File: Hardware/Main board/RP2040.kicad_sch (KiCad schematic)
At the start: 16 parts, among them U4 RP2040

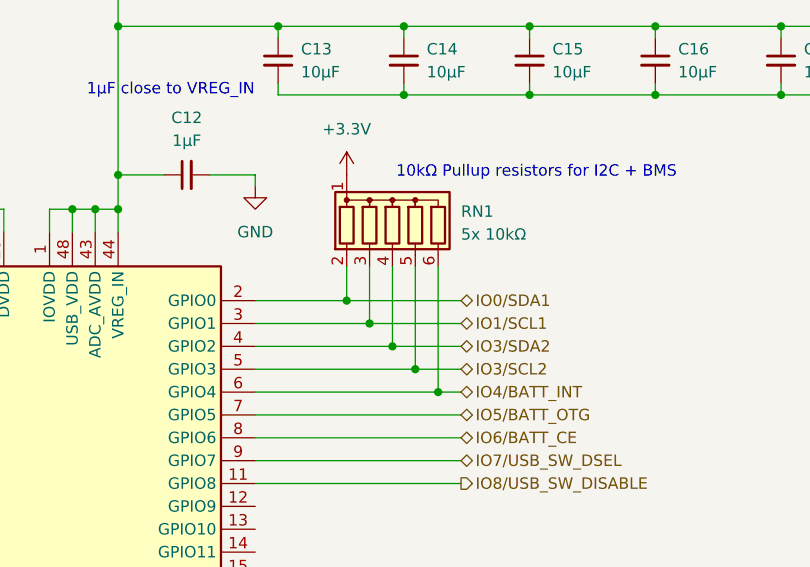
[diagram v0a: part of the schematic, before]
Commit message: Big changes
- Folder changes
- change dimensions of board to match thicker material
- begin part selection/footprint selection
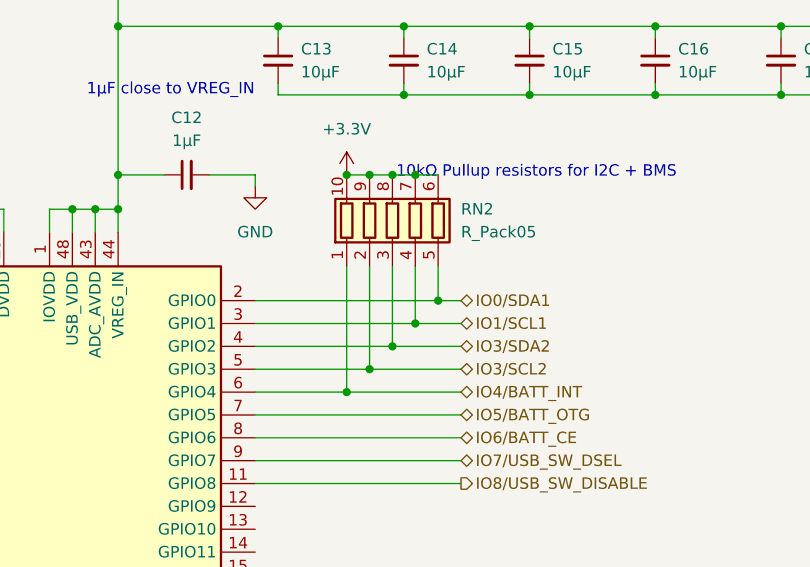
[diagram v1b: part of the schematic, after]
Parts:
- removed RN1: 5x 10kΩ, Resistor_THT:R_Array_SIP6, symbol Device:R_Network05
- added RN2: R_Pack05, Resistor_SMD:R_Array_Convex_5x0603, symbol Device:R_Pack05
- C10, C13, C14, C15, C16, C17, C18, C19, C20, C9: footprint (none) -> Capacitor_SMD:C_0603_1608Metric
- C11, C12: footprint (none) -> Capacitor_SMD:C_0402_1005Metric
- R5, R6: footprint (none) -> Resistor_SMD:R_0603_1608Metric
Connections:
- net +3.3V: now also RN2.10 (R1.2), RN2.6 (R5.2), RN2.7 (R4.2), RN2.8 (R3.2), RN2.9 (R2.2)
- net IO0/SDA1: now also RN2.5 (R5.1)
- net IO1/SCL1: now also RN2.4 (R4.1)
- net IO3/SCL2: now also RN2.2 (R2.1)
- net IO3/SDA2: now also RN2.3 (R3.1)
- net IO4/BATT_INT: now also RN2.1 (R1.1)

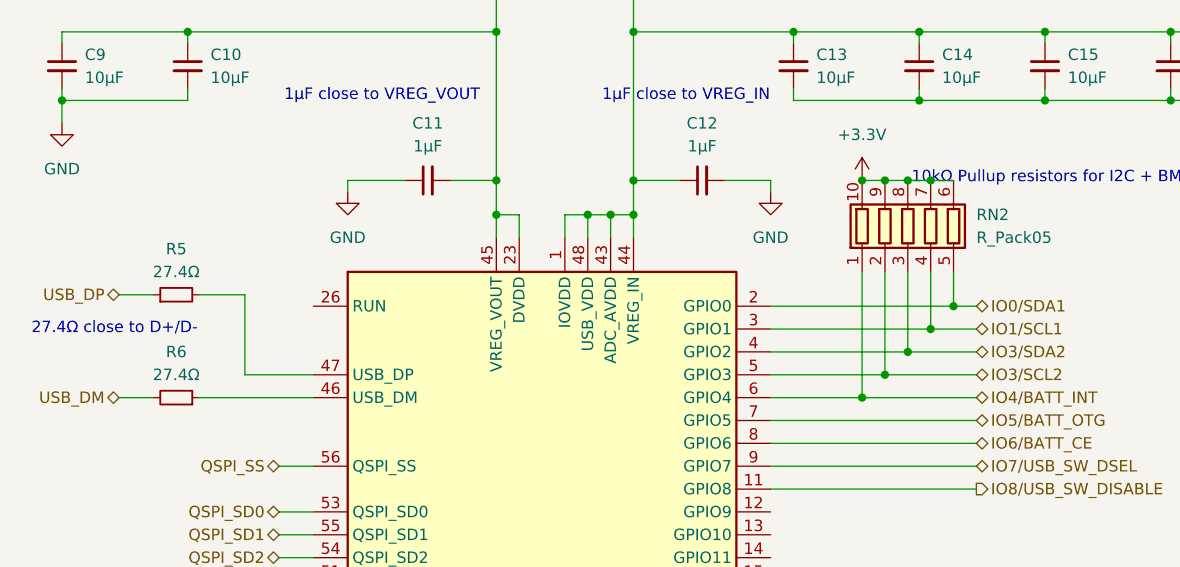
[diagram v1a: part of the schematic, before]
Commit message: Schematic changes
- changed positions/schematic values and nets
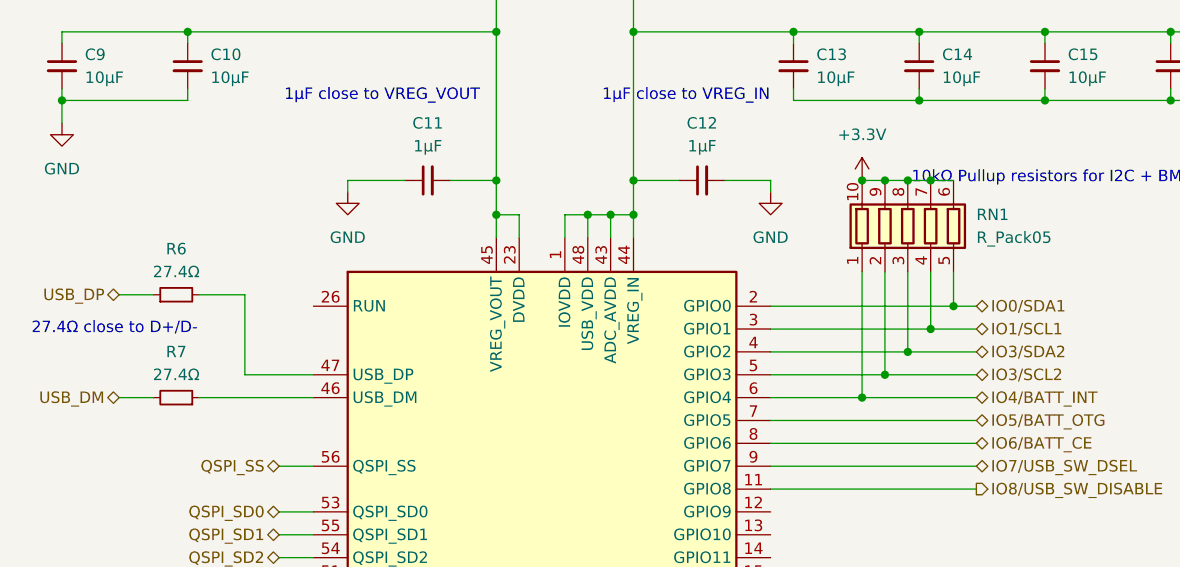
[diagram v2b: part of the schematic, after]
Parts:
- renumbered R5 to R6, R6 to R7, RN2 to RN1
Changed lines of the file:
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@@
 		(dnp no)
 		(fields_autoplaced yes)
-		(property "Reference" "#PWR030"
+		(property "Reference" "#PWR028"
 			(at 106.68 162.56 0)
 			(effects
@@
 			(project "Minibadge Display 5x3"
 				(path "/e5119d15-74fb-4259-abbc-5cab1f368532/9c03ac80-c552-4a59-83c4-4e8b67a63031"
-					(reference "#PWR030")
+					(reference "#PWR028")
 					(unit 1)
 				)
@@
 		(dnp no)
 		(fields_autoplaced yes)
-		(property "Reference" "RN2"
+		(property "Reference" "RN1"
 			(at 154.94 62.2299 0)
 			(effects
@@
 			(project ""
 				(path "/e5119d15-74fb-4259-abbc-5cab1f368532/9c03ac80-c552-4a59-83c4-4e8b67a63031"
-					(reference "RN2")
+					(reference "RN1")
 					(unit 1)
 				)
@@
 		(dnp no)
 		(fields_autoplaced yes)
-		(property "Reference" "#PWR029"
+		(property "Reference" "#PWR027"
 			(at 101.6 38.1 0)
 			(effects
@@
 			(project ""
 				(path "/e5119d15-74fb-4259-abbc-5cab1f368532/9c03ac80-c552-4a59-83c4-4e8b67a63031"
-					(reference "#PWR029")
+					(reference "#PWR027")
 					(unit 1)
 				)
@@
 		(dnp no)
 		(fields_autoplaced yes)
-		(property "Reference" "#PWR033"
+		(property "Reference" "#PWR031"
 			(at 142.24 62.23 0)
 			(effects
@@
 			(project ""
 				(path "/e5119d15-74fb-4259-abbc-5cab1f368532/9c03ac80-c552-4a59-83c4-4e8b67a63031"
-					(reference "#PWR033")
+					(reference "#PWR031")
 					(unit 1)
 				)
@@
 		(dnp no)
 		(fields_autoplaced yes)
-		(property "Reference" "#PWR034"
+		(property "Reference" "#PWR032"
 			(at 232.41 58.42 0)
 			(effects
@@
 			(project ""
 				(path "/e5119d15-74fb-4259-abbc-5cab1f368532/9c03ac80-c552-4a59-83c4-4e8b67a63031"
-					(reference "#PWR034")
+					(reference "#PWR032")
 					(unit 1)
 				)
@@
 		(dnp no)
 		(fields_autoplaced yes)
-		(property "Reference" "#PWR032"
+		(property "Reference" "#PWR030"
 			(at 132.08 66.04 0)
 			(effects
@@
 			(project "Minibadge Display 5x3"
 				(path "/e5119d15-74fb-4259-abbc-5cab1f368532/9c03ac80-c552-4a59-83c4-4e8b67a63031"
-					(reference "#PWR032")
+					(reference "#PWR030")
 					(unit 1)
 				)
@@
 		(on_board yes)
 		(dnp no)
-		(property "Reference" "R6"
+		(property "Reference" "R7"
 			(at 66.04 77.47 90)
 			(effects
@@
 			(project ""
 				(path "/e5119d15-74fb-4259-abbc-5cab1f368532/9c03ac80-c552-4a59-83c4-4e8b67a63031"
-					(reference "R6")
+					(reference "R7")
 					(unit 1)
 				)
@@
 		(dnp no)
 		(fields_autoplaced yes)
-		(property "Reference" "#PWR028"
+		(property "Reference" "#PWR026"
 			(at 85.09 66.04 0)
 			(effects
@@
 			(project "Minibadge Display 5x3"
 				(path "/e5119d15-74fb-4259-abbc-5cab1f368532/9c03ac80-c552-4a59-83c4-4e8b67a63031"
-					(reference "#PWR028")
+					(reference "#PWR026")
 					(unit 1)
 				)
@@
 		(dnp no)
 		(fields_autoplaced yes)
-		(property "Reference" "#PWR027"
+		(property "Reference" "#PWR025"
 			(at 53.34 58.42 0)
 			(effects
@@
 			(project ""
 				(path "/e5119d15-74fb-4259-abbc-5cab1f368532/9c03ac80-c552-4a59-83c4-4e8b67a63031"
-					(reference "#PWR027")
+					(reference "#PWR025")
 					(unit 1)
 				)
@@
 		(dnp no)
 		(fields_autoplaced yes)
-		(property "Reference" "#PWR031"
+		(property "Reference" "#PWR029"
 			(at 116.84 38.1 0)
 			(effects
@@
 			(project ""
 				(path "/e5119d15-74fb-4259-abbc-5cab1f368532/9c03ac80-c552-4a59-83c4-4e8b67a63031"
-					(reference "#PWR031")
+					(reference "#PWR029")
 					(unit 1)
 				)
@@
 		(dnp no)
 		(fields_autoplaced yes)
-		(property "Reference" "R5"
+		(property "Reference" "R6"
 			(at 66.04 66.04 90)
 			(effects
@@
 			(project ""
 				(path "/e5119d15-74fb-4259-abbc-5cab1f368532/9c03ac80-c552-4a59-83c4-4e8b67a63031"
-					(reference "R5")
-					(unit 1)
-				)
+					(reference "R6")
+					(unit 1)
+				)

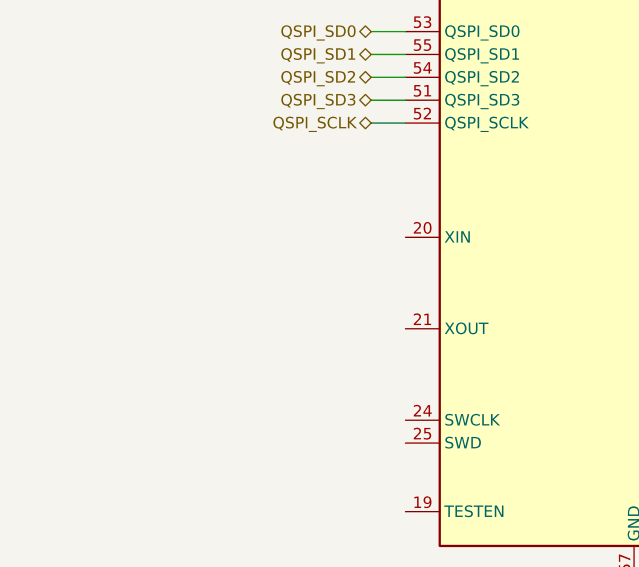
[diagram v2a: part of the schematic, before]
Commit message: Routed Minibadge Display
god that sucked, and my routing sucks too.
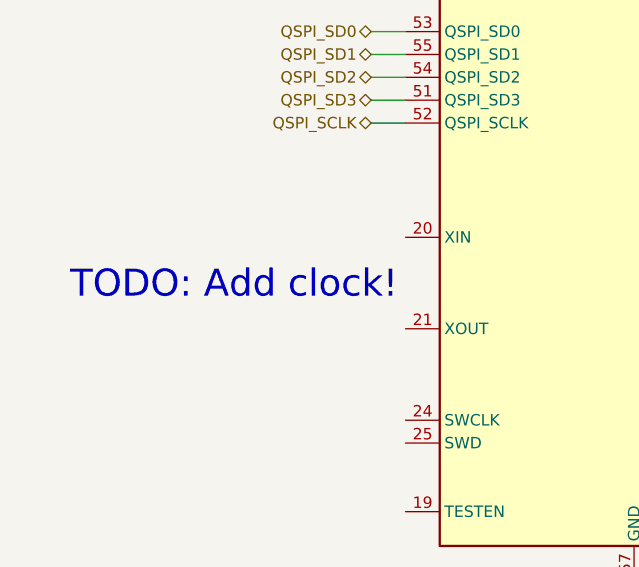
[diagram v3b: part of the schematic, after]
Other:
- note added: "TODO: Add clock!"
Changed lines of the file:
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@@
+		)
+	)
+	(text "TODO: Add clock!"
+		(exclude_from_sim no)
+		(at 62.23 123.444 0)
+		(effects
+			(font
+				(size 3 3)
+			)
 		)
 	)

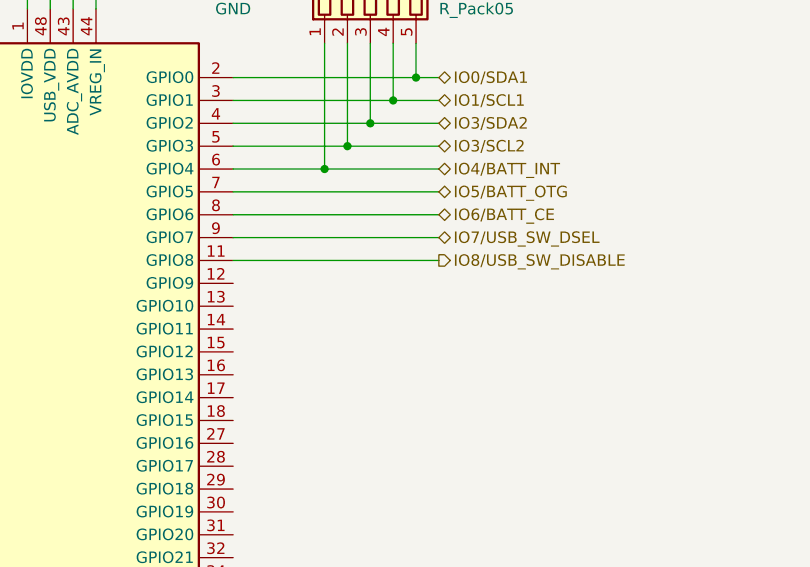
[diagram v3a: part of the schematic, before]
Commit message: Add Voltage Regulators
TLV1117LV33
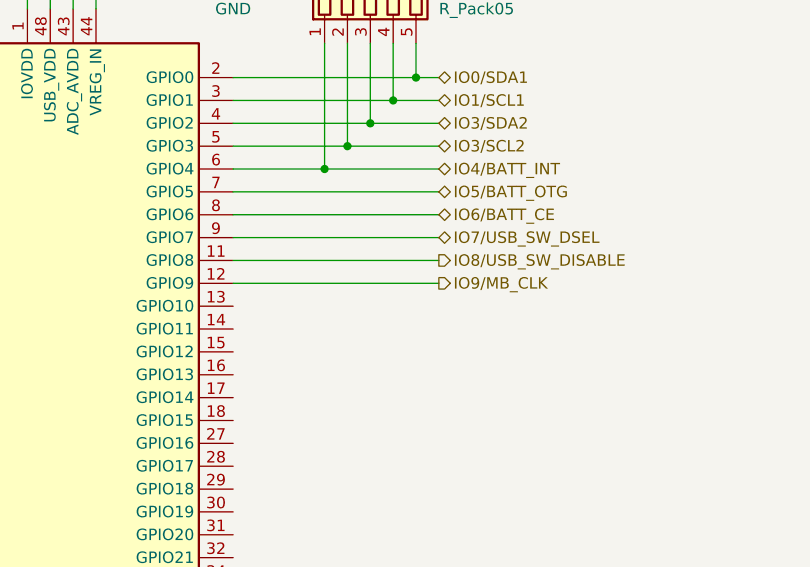
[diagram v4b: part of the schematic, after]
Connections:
- net IO9/MB_CLK: now reaches U4.12 (GPIO9)
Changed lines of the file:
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@@
+	(wire
+		(pts
+			(xy 154.94 95.25) (xy 132.08 95.25)
+		)
+		(stroke
+			(width 0)
+			(type default)
+		)
+	)
 	(wire
 		(pts
@@
 		)
 	)
+	(hierarchical_label "IO9{slash}MB_CLK"
+		(shape output)
+		(at 154.94 95.25 0)
+		(effects
+			(font
+				(size 1.27 1.27)
+			)
+			(justify left)
+		)
+	)

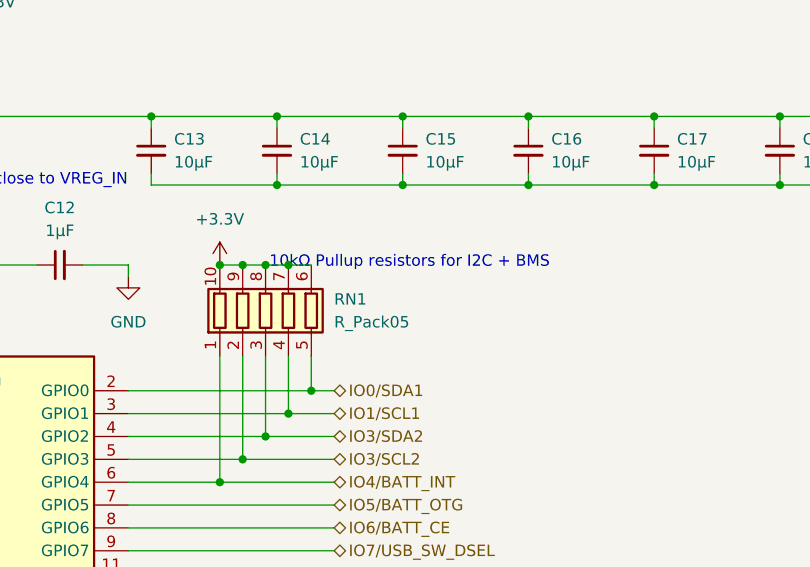
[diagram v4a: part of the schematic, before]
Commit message: hardware changes and initial traces/layout
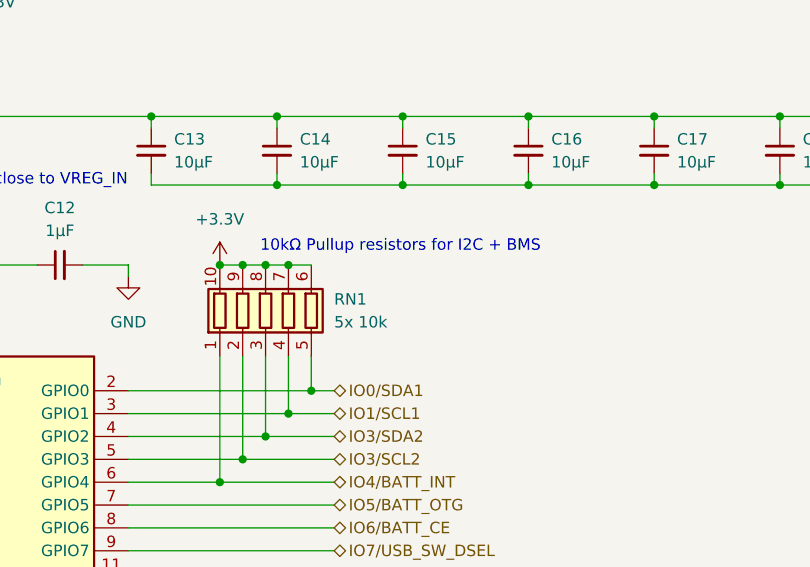
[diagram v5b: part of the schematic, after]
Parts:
- RN1: value R_Pack05 -> 5x 10k
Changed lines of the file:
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@@
 	(text "10kΩ Pullup resistors for I2C + BMS"
 		(exclude_from_sim no)
-		(at 163.322 58.166 0)
+		(at 162.306 56.388 0)
 		(effects
 			(font
@@
 			)
 		)
-		(property "Value" "R_Pack05"
+		(property "Value" "5x 10k"
 			(at 154.94 64.7699 0)
 			(effects

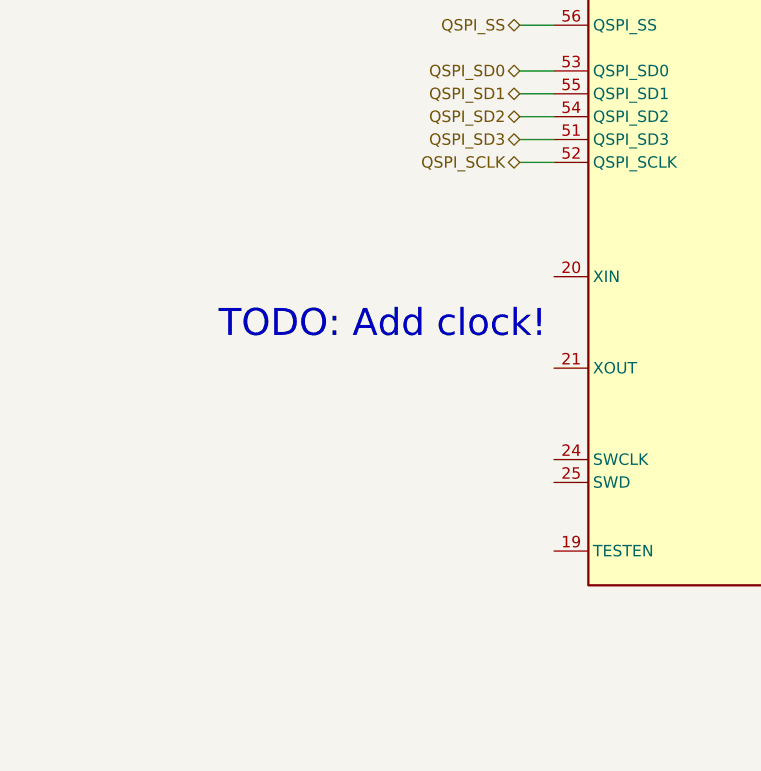
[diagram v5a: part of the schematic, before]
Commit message: Add Crystal
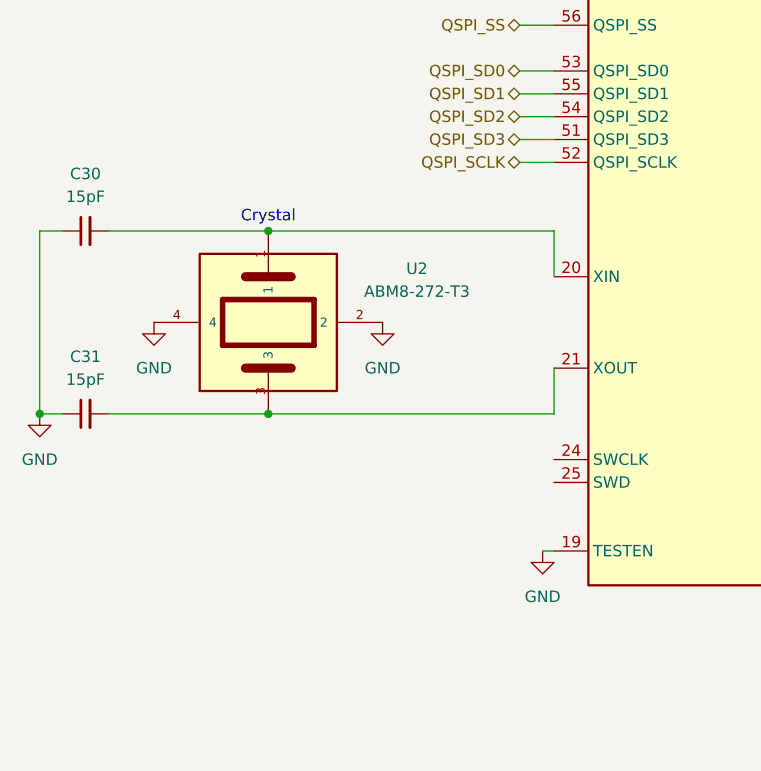
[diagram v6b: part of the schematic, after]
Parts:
- added C30, C31: 15pF, Capacitor_SMD:C_0402_1005Metric, symbol Device:C_Small
- added U2: ABM8-272-T3, Crystal:Crystal_SMD_Abracon_ABM8G-4Pin_3.2x2.5mm, symbol ABM8-272-T3:ABM8-272-T3
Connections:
- net GND: now also U4.19 (TESTEN), C30.1, C31.1, U2.2, U2.4
- net at U4.20 (XIN): now also C30.2, U2.1
- net at U4.21 (XOUT): now also C31.2, U2.3
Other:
- note added: "Crystal"
- note removed: "TODO: Add clock!"

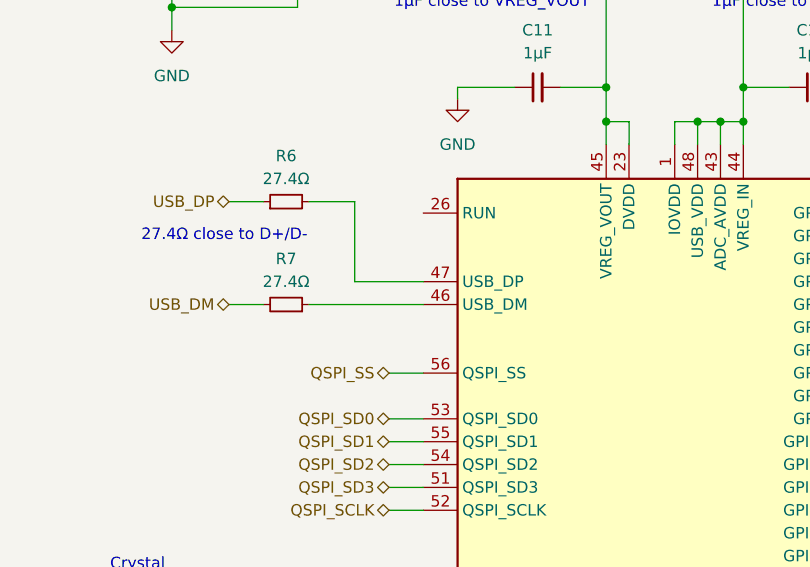
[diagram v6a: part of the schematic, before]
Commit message: 1st semi complete board layout
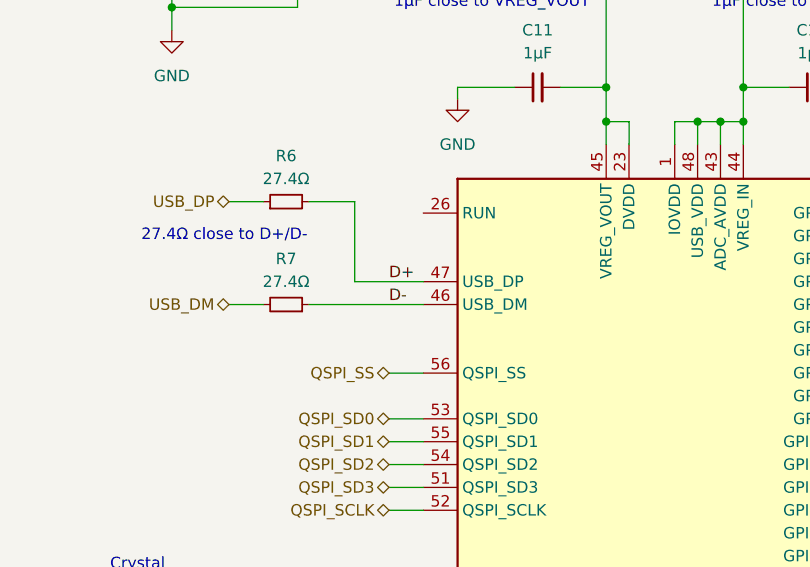
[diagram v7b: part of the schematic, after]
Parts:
- R6, R7: footprint Resistor_SMD:R_0603_1608Metric -> Resistor_SMD:R_0402_1005Metric
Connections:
- net D-: now reaches R7.1, U4.46 (USB_DM)
- net D+: now reaches R6.2, U4.47 (USB_DP)
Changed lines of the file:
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@@
+		)
+	)
+	(label "D+"
+		(at 77.47 80.01 0)
+		(effects
+			(font
+				(size 1.27 1.27)
+			)
+			(justify left bottom)
+		)
+	)
+	(label "D-"
+		(at 77.47 82.55 0)
+		(effects
+			(font
+				(size 1.27 1.27)
+			)
+			(justify left bottom)
 		)
 	)
@@
 			)
 		)
-		(property "Footprint" "Resistor_SMD:R_0603_1608Metric"
+		(property "Footprint" "Resistor_SMD:R_0402_1005Metric"
 			(at 66.04 82.55 0)
 			(effects
@@
 			)
 		)
-		(property "Footprint" "Resistor_SMD:R_0603_1608Metric"
+		(property "Footprint" "Resistor_SMD:R_0402_1005Metric"
 			(at 66.04 71.12 0)
 			(effects
